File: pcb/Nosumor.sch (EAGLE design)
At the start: 124 parts, among them IC1 STM32F722RET, J4 SJ-43515TS-SMT-EDGE, K1 CHERRY-MX, K2 CHERRY-MX, K3 KSC623J, K4 KSC623J, K5 KSC623J, Q1 ABM8W-12.0000MHZ, Q2 CX2016DB, Q3 FDY100PZ, Q4 FDY100PZ, Q5 FDY100PZ, Q6 FDY100PZ, U1 3.3V, U2 FT2232H-56Q-REEL, U3 3.3V, U4 24CW1280T-I/OT, U5 9DoF IMU, U6 3.3V, U7 USB3370, U8 TLV320AIC3256

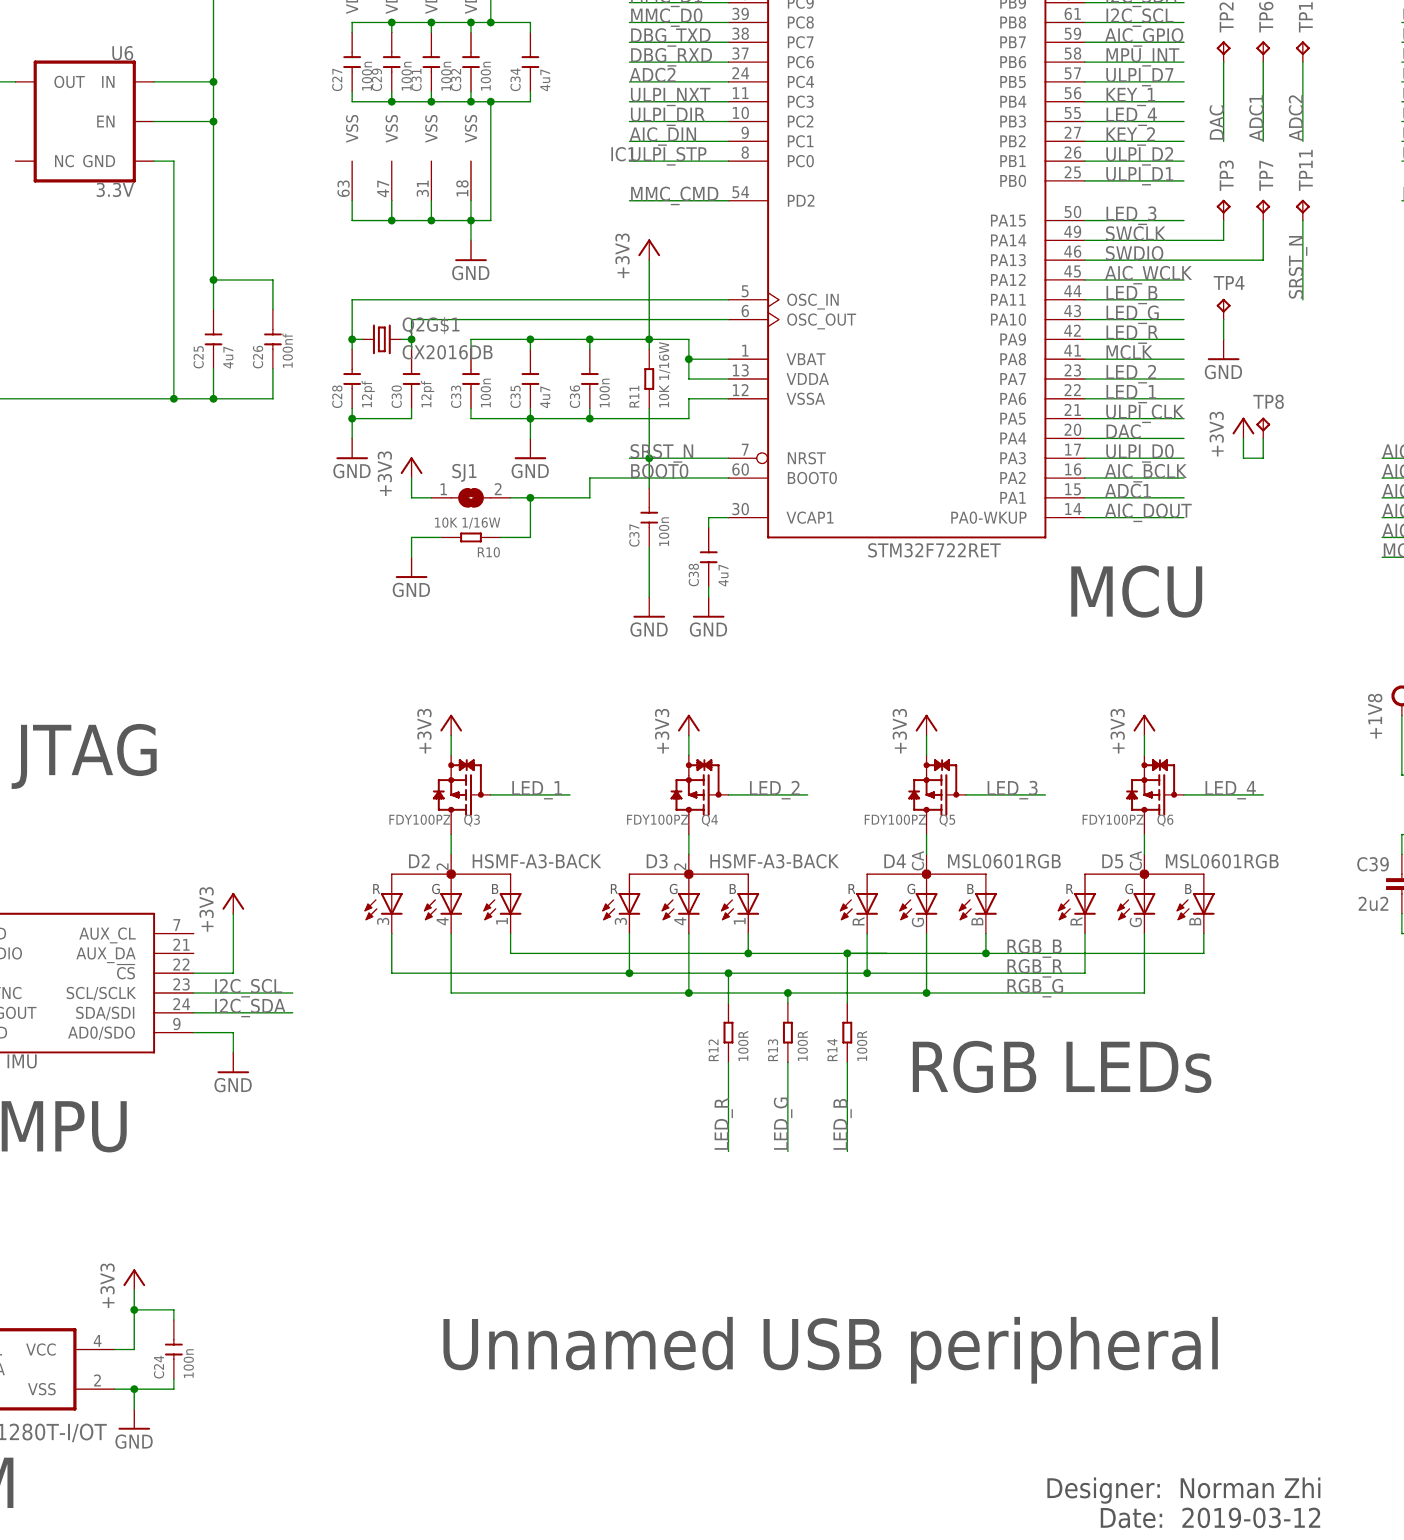
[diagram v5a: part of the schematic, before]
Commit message: Update PCB BOM, fix miscellaneous schematic markings
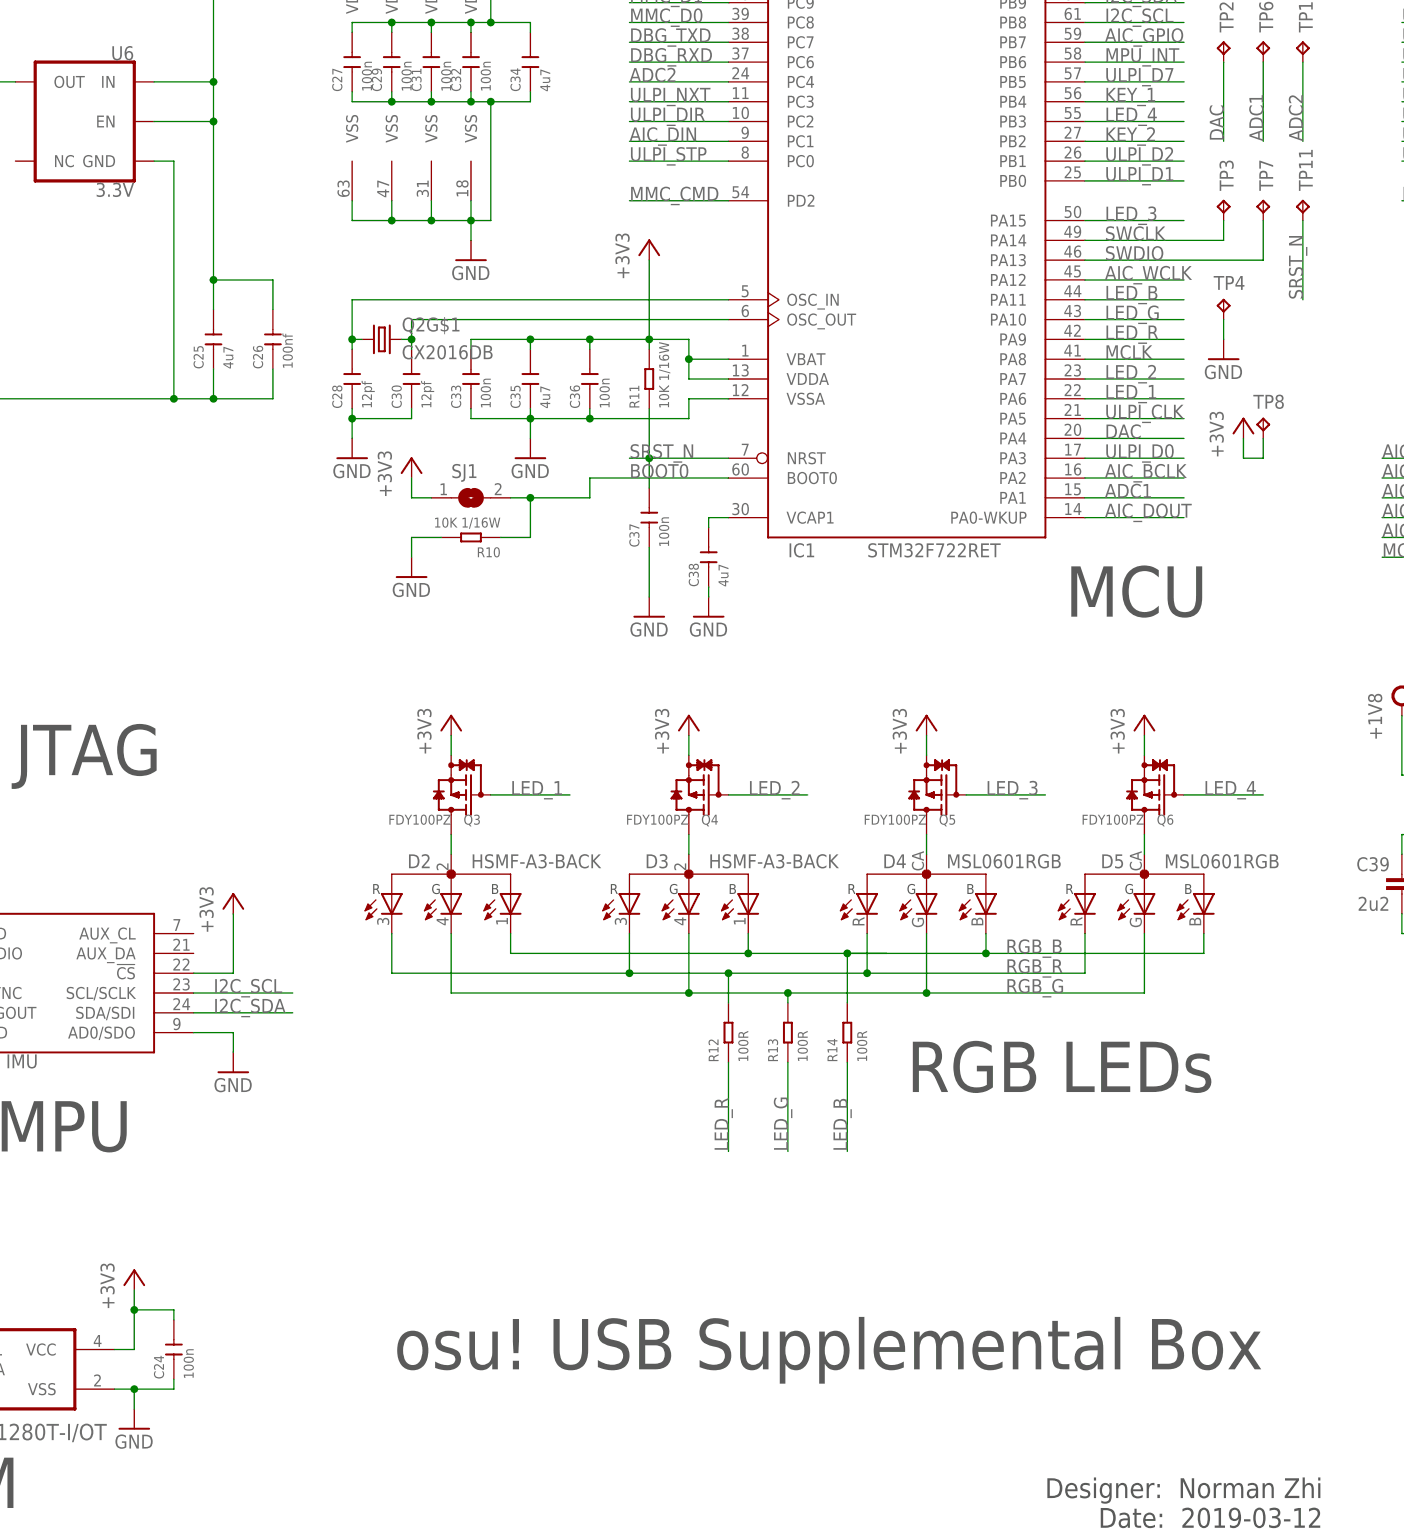
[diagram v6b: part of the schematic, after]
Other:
- note added: "osu! USB Supplemental Box"
- note removed: "Unnamed USB peripheral"
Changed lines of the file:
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@@
 <?xml version="1.0" encoding="utf-8"?>
 <!DOCTYPE eagle SYSTEM "eagle.dtd">
-<eagle version="9.3.1">
+<eagle version="9.3.2">
 <drawing>
 <settings>
@@
 <text x="302.26" y="2.54" size="2.54" layer="97" align="bottom-right">Designer:  Norman Zhi
 Date:  2019-03-12</text>
-<text x="289.56" y="22.86" size="6.4516" layer="97" align="bottom-right">Unnamed USB peripheral</text>
+<text x="294.64" y="22.86" size="6.4516" layer="97" align="bottom-right">osu! USB Supplemental Box</text>
 </plain>
 <instances>
@@
 </instance>
 <instance part="IC1" gate="G$1" x="248.92" y="172.72" smashed="yes">
-<attribute name="NAME" x="210.82" y="177.8" size="1.778" layer="95"/>
+<attribute name="NAME" x="233.68" y="127" size="1.778" layer="95"/>
 <attribute name="VALUE" x="243.84" y="127" size="1.778" layer="96"/>
 </instance>

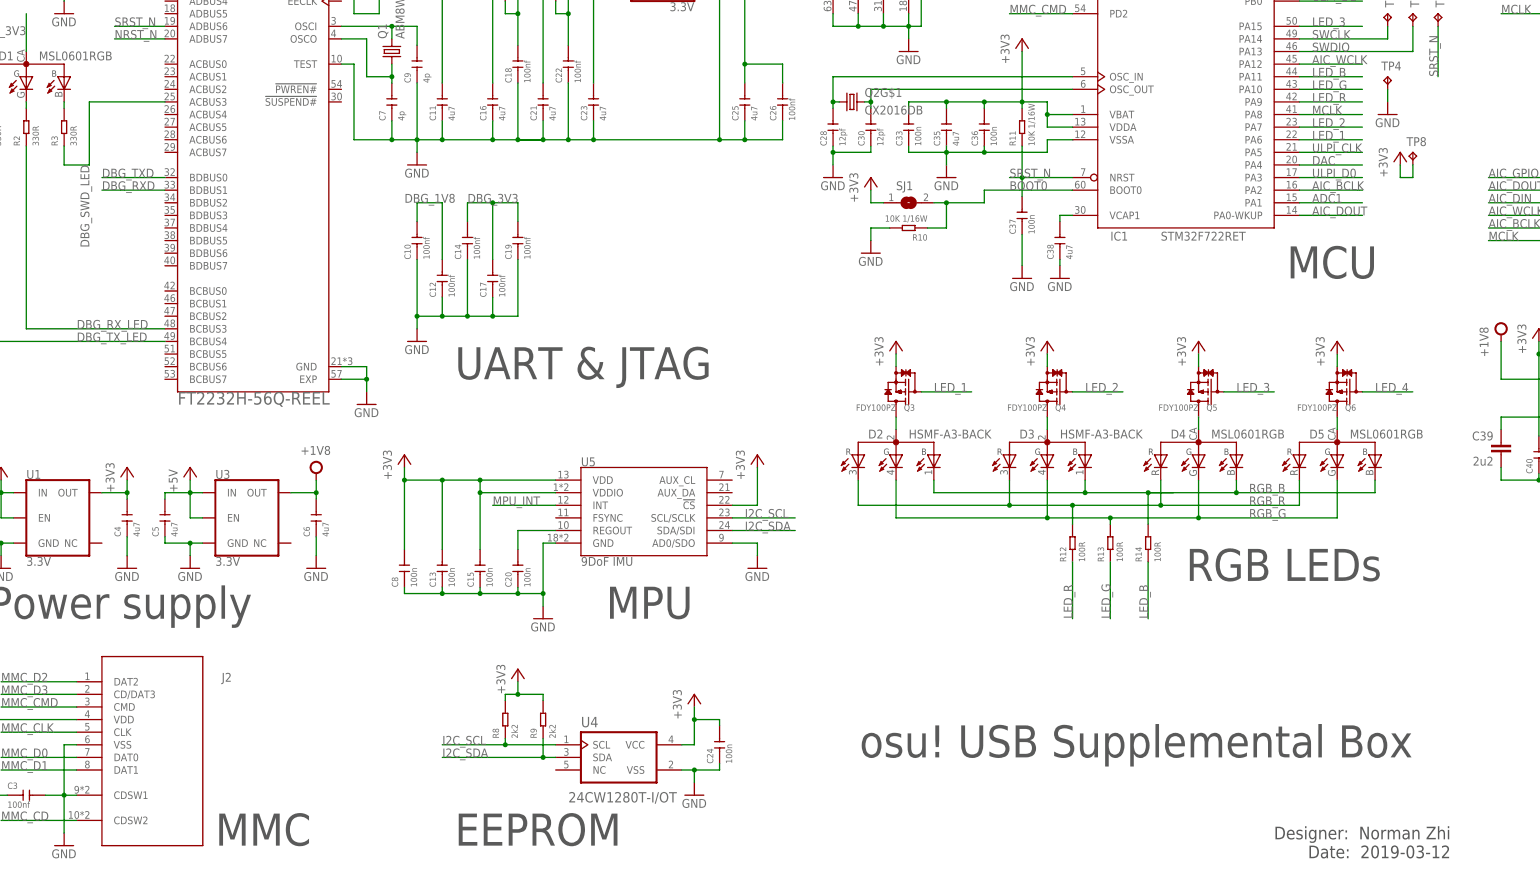
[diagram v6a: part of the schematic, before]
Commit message: PCB revision 1.2, fix RGB LED footprint
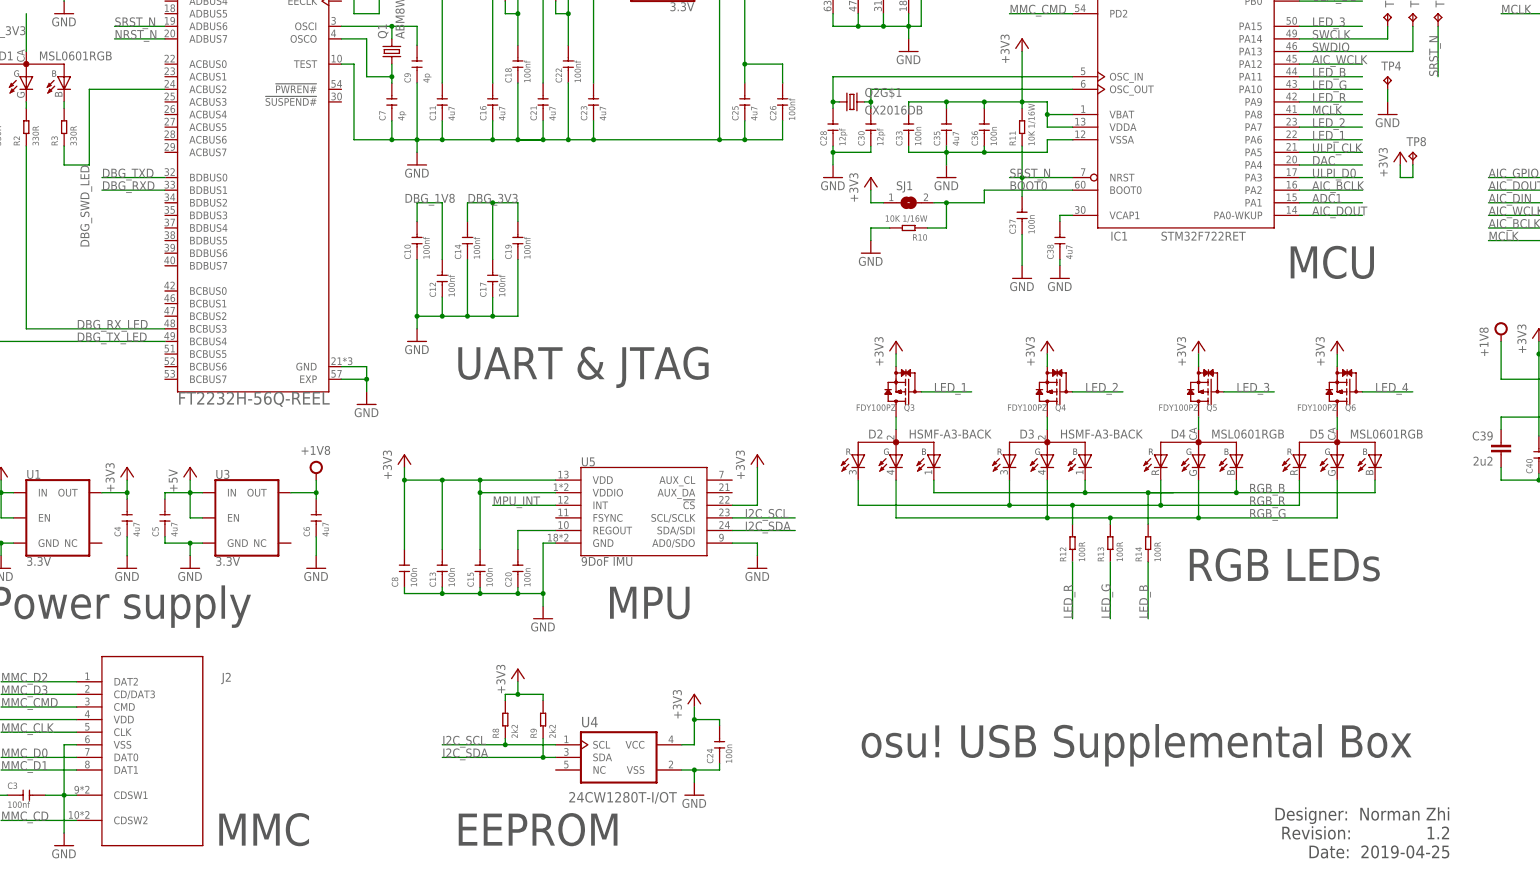
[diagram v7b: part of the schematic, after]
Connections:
- net DBG_SWD_LED: now also U2.ACBUS2; no longer U2.ACBUS3
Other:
- note added: "Designer: Norman Zhi Revision: 1.2 Date: 2019-04-25"
- note removed: "Designer: Norman Zhi Date: 2019-03-12"
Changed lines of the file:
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@@
 <?xml version="1.0" encoding="utf-8"?>
 <!DOCTYPE eagle SYSTEM "eagle.dtd">
-<eagle version="9.3.2">
+<eagle version="9.4.0">
 <drawing>
 <settings>
@@
 <wire x1="172.72" y1="0" x2="304.8" y2="0" width="2.54" layer="90"/>
 <text x="302.26" y="2.54" size="2.54" layer="97" align="bottom-right">Designer:  Norman Zhi
-Date:  2019-03-12</text>
+Revision:               1.2
+Date:  2019-04-25</text>
 <text x="294.64" y="22.86" size="6.4516" layer="97" align="bottom-right">osu! USB Supplemental Box</text>
 </plain>
@@
 <wire x1="22.86" y1="146.05" x2="22.86" y2="142.24" width="0.1524" layer="91"/>
 <wire x1="22.86" y1="142.24" x2="27.94" y2="142.24" width="0.1524" layer="91"/>
-<pinref part="U2" gate="G$1" pin="ACBUS3"/>
-<wire x1="27.94" y1="142.24" x2="27.94" y2="154.94" width="0.1524" layer="91"/>
-<wire x1="27.94" y1="154.94" x2="43.18" y2="154.94" width="0.1524" layer="91"/>
+<wire x1="27.94" y1="142.24" x2="27.94" y2="157.48" width="0.1524" layer="91"/>
 <label x="27.94" y="142.24" size="1.778" layer="255" rot="MR270"/>
+<pinref part="U2" gate="G$1" pin="ACBUS2"/>
+<wire x1="43.18" y1="157.48" x2="27.94" y2="157.48" width="0.1524" layer="91"/>
 </segment>
 </net>
@@
 </sheet>
 </sheets>
-<errors>
-</errors>
 </schematic>
 </drawing>
